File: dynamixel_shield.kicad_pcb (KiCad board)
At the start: 2 copper layers, 68.6 x 53.3 mm, 27 parts, among them P1 BARREL_JACK, P2 CONN_01X02, P3 CONN_01X03, P4 CONN_01X03, P5 CONN_01X03, P6 CONN_01X03, P7 CONN_01X03, P8 CONN_01X03, P9 CONN_01X03, Q1 MOSFET_N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

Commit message: change capacitor height (bom related only, footprint is the same)
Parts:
- C1: footprint Capacitors_SMD:c_elec_6.3x5.3 -> Capacitors_SMD:c_elec_6.3x5.8
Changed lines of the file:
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@@
     (links 61)
     (no_connects 0)
-    (area 53.318999 50.945 132.842001 112.522001)
+    (area 0 0 0 0)
     (thickness 1.6)
     (drawings 20)
@@
       (xy 0.633953 3.996765) (xy 0.746536 3.399573)) (layer B.Cu) (width 0.01))
   )
-  (module Capacitors_SMD:c_elec_6.3x5.3 (layer F.Cu)
-    (at 93.98 84.328)
-    (descr "SMT capacitor, aluminium electrolytic, 6.3x5.3")
-    (attr smd)
-    (fp_text reference C1 (at 0 -4.445) (layer F.SilkS)
-      (effects (font (size 1 1) (thickness 0.15)))
-    )
-    (fp_text value 47uF (at 0 4.445) (layer F.Fab)
-      (effects (font (size 1 1) (thickness 0.15)))
-    )
-    (fp_line (start -4.85 -3.65) (end 4.85 -3.65) (layer F.CrtYd) (width 0.05))
-    (fp_line (start 4.85 -3.65) (end 4.85 3.65) (layer F.CrtYd) (width 0.05))
-    (fp_line (start 4.85 3.65) (end -4.85 3.65) (layer F.CrtYd) (width 0.05))
-    (fp_line (start -4.85 3.65) (end -4.85 -3.65) (layer F.CrtYd) (width 0.05))
-    (fp_line (start -2.921 -0.762) (end -2.921 0.762) (layer F.SilkS) (width 0.15))
-    (fp_line (start -2.794 1.143) (end -2.794 -1.143) (layer F.SilkS) (width 0.15))
-    (fp_line (start -2.667 -1.397) (end -2.667 1.397) (layer F.SilkS) (width 0.15))
-    (fp_line (start -2.54 1.651) (end -2.54 -1.651) (layer F.SilkS) (width 0.15))
-    (fp_line (start -2.413 -1.778) (end -2.413 1.778) (layer F.SilkS) (width 0.15))
-    (fp_line (start -3.302 -3.302) (end -3.302 3.302) (layer F.SilkS) (width 0.15))
-    (fp_line (start -3.302 3.302) (end 2.54 3.302) (layer F.SilkS) (width 0.15))
-    (fp_line (start 2.54 3.302) (end 3.302 2.54) (layer F.SilkS) (width 0.15))
-    (fp_line (start 3.302 2.54) (end 3.302 -2.54) (layer F.SilkS) (width 0.15))
-    (fp_line (start 3.302 -2.54) (end 2.54 -3.302) (layer F.SilkS) (width 0.15))
-    (fp_line (start 2.54 -3.302) (end -3.302 -3.302) (layer F.SilkS) (width 0.15))
-    (fp_line (start 2.159 0) (end 1.397 0) (layer F.SilkS) (width 0.15))
-    (fp_line (start 1.778 -0.381) (end 1.778 0.381) (layer F.SilkS) (width 0.15))
-    (fp_circle (center 0 0) (end -3.048 0) (layer F.SilkS) (width 0.15))
-    (pad 1 smd rect (at 2.75082 0) (size 3.59918 1.6002) (layers F.Cu F.Paste F.Mask)
-      (net 9 +12V))
-    (pad 2 smd rect (at -2.75082 0) (size 3.59918 1.6002) (layers F.Cu F.Paste F.Mask)
-      (net 11 GND))
-    (model Capacitors_SMD.3dshapes/c_elec_6.3x5.3.wrl
-      (at (xyz 0 0 0))
-      (scale (xyz 1 1 1))
-      (rotate (xyz 0 0 0))
-    )
-  )
   (module Pin_Headers:Pin_Header_Straight_1x04 (layer F.Cu)
     (at 104.648 65.024 270)
@@
       (net 33 "Net-(SHIELD1-PadSCL)"))
   )
+  (module Capacitors_SMD:c_elec_6.3x5.8 (layer F.Cu)
+    (at 93.98 84.328)
+    (descr "SMT capacitor, aluminium electrolytic, 6.3x5.8")
+    (attr smd)
+    (fp_text reference C1 (at 0 -4.445) (layer F.SilkS)
+      (effects (font (size 1 1) (thickness 0.15)))
+    )
+    (fp_text value 47uF (at 0 4.445) (layer F.Fab)
+      (effects (font (size 1 1) (thickness 0.15)))
+    )
+    (fp_line (start -4.85 -3.65) (end 4.85 -3.7) (layer F.CrtYd) (width 0.05))
+    (fp_line (start 4.85 -3.7) (end 4.85 3.65) (layer F.CrtYd) (width 0.05))
+    (fp_line (start 4.85 3.65) (end -4.85 3.65) (layer F.CrtYd) (width 0.05))
+    (fp_line (start -4.85 3.65) (end -4.85 -3.65) (layer F.CrtYd) (width 0.05))
+    (fp_line (start -2.921 -0.762) (end -2.921 0.762) (layer F.SilkS) (width 0.15))
+    (fp_line (start -2.794 1.143) (end -2.794 -1.143) (layer F.SilkS) (width 0.15))
+    (fp_line (start -2.667 -1.397) (end -2.667 1.397) (layer F.SilkS) (width 0.15))
+    (fp_line (start -2.54 1.651) (end -2.54 -1.651) (layer F.SilkS) (width 0.15))
+    (fp_line (start -2.413 -1.778) (end -2.413 1.778) (layer F.SilkS) (width 0.15))
+    (fp_line (start -3.302 -3.302) (end -3.302 3.302) (layer F.SilkS) (width 0.15))
+    (fp_line (start -3.302 3.302) (end 2.54 3.302) (layer F.SilkS) (width 0.15))
+    (fp_line (start 2.54 3.302) (end 3.302 2.54) (layer F.SilkS) (width 0.15))
+    (fp_line (start 3.302 2.54) (end 3.302 -2.54) (layer F.SilkS) (width 0.15))
+    (fp_line (start 3.302 -2.54) (end 2.54 -3.302) (layer F.SilkS) (width 0.15))
+    (fp_line (start 2.54 -3.302) (end -3.302 -3.302) (layer F.SilkS) (width 0.15))
+    (fp_line (start 2.159 0) (end 1.397 0) (layer F.SilkS) (width 0.15))
+    (fp_line (start 1.778 -0.381) (end 1.778 0.381) (layer F.SilkS) (width 0.15))
+    (fp_circle (center 0 0) (end -3.048 0) (layer F.SilkS) (width 0.15))
+    (pad 1 smd rect (at 2.75082 0) (size 3.59918 1.6002) (layers F.Cu F.Paste F.Mask)
+      (net 9 +12V))
+    (pad 2 smd rect (at -2.75082 0) (size 3.59918 1.6002) (layers F.Cu F.Paste F.Mask)
+      (net 11 GND))
+    (model Capacitors_SMD.3dshapes/c_elec_6.3x5.8.wrl
+      (at (xyz 0 0 0))
+      (scale (xyz 1 1 1))
+      (rotate (xyz 0 0 0))
+    )
+  )
   (gr_text EXT (at 115.57 65.532 90) (layer F.SilkS)

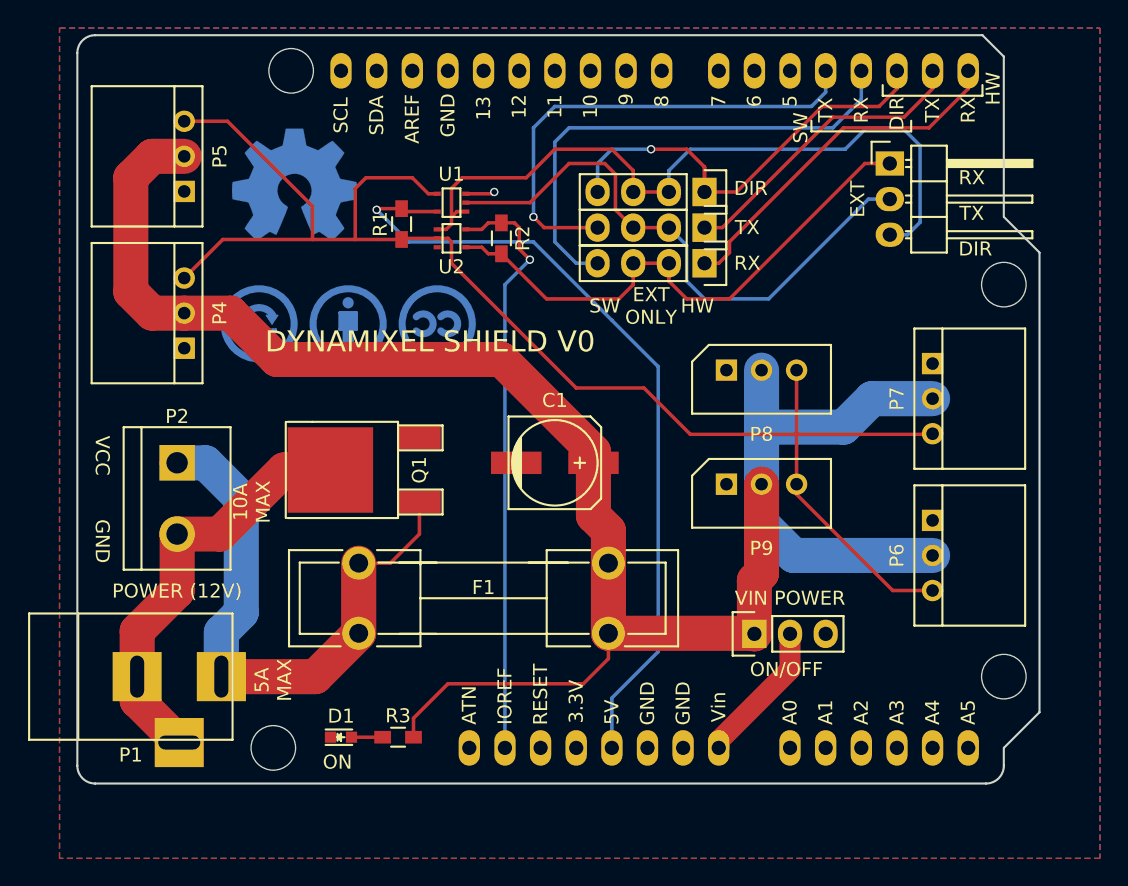
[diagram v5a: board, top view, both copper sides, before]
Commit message: fix a few shortcomings of the pcb, thanks to tautech from eevblog forum
remove potential acid trap between p8 and p9
increase pad size of molex connectors
move polarity indicators to be visible
increase led pad size for easier soldering
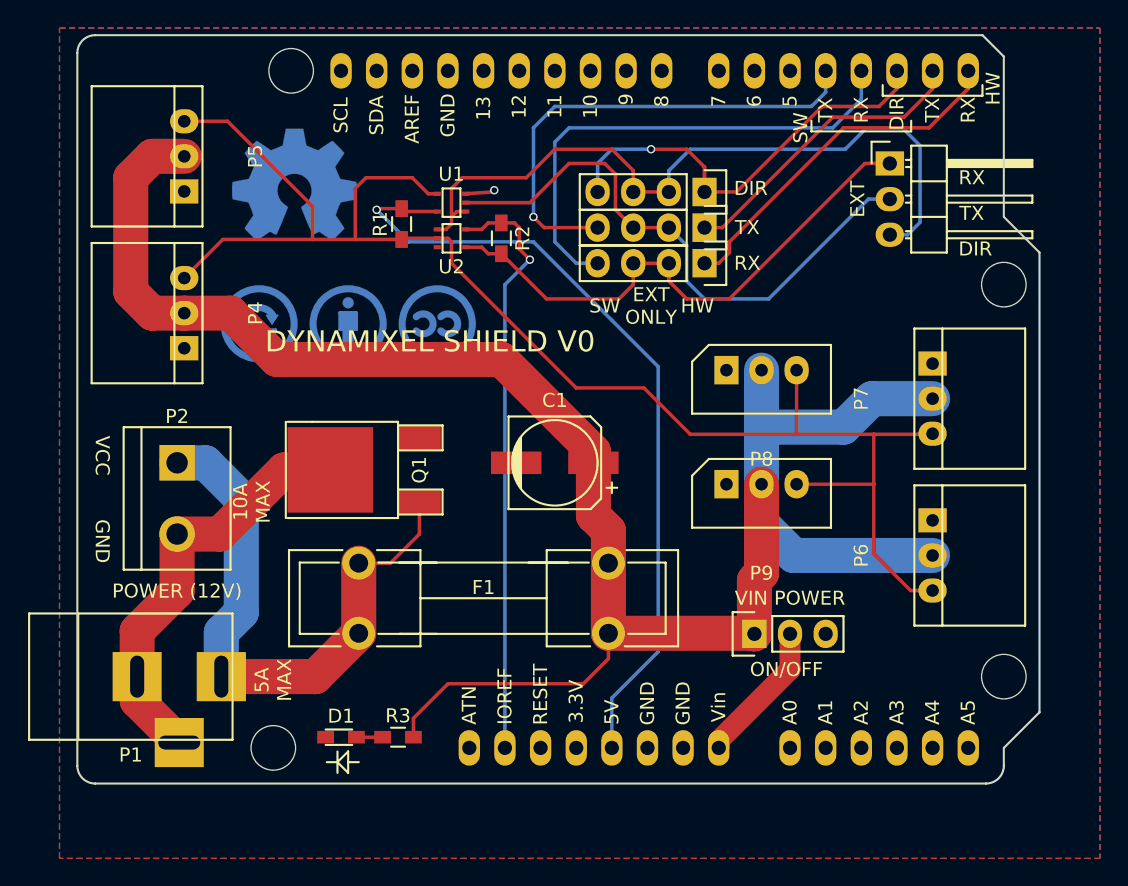
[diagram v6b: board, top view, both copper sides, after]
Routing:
- net /DATA: track 107.0 -> 109.5 mm
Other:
- board text removed: "ON"

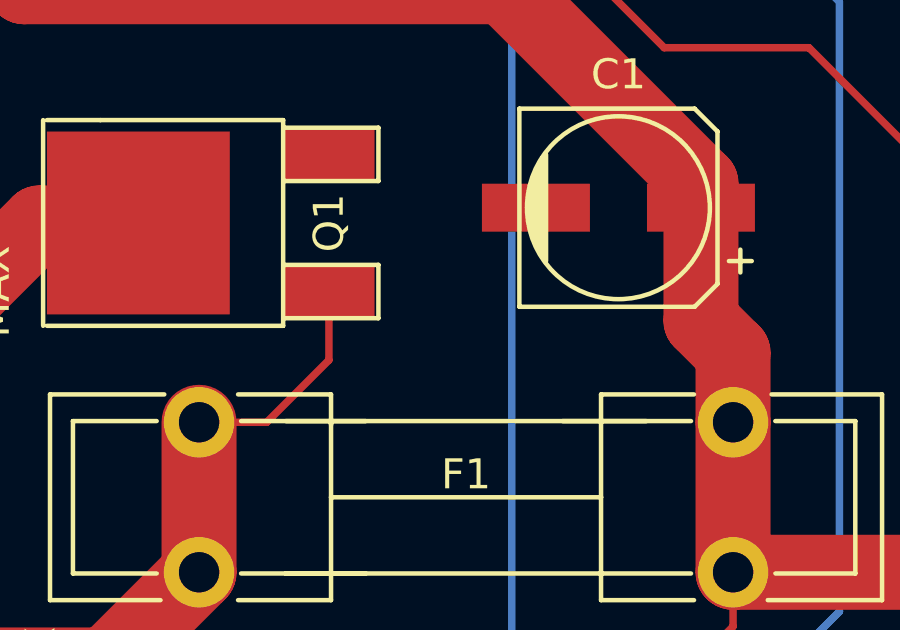
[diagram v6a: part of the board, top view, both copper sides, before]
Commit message: put the fuse before the reverse voltage protection (thanks to bktemp from eevblog forum)
Quoting bktemp user on eevblog:

When the fuse fails, there will be a voltage spike.
Since there is no load except the mosfet gate, the voltage spike will damage the mosfet,
maybe even shorting gate-source and therefore the input supply.
If the gate is connected after the fuse, is will be connected in parallel with C1,
providing some protection for the sensitive gate.
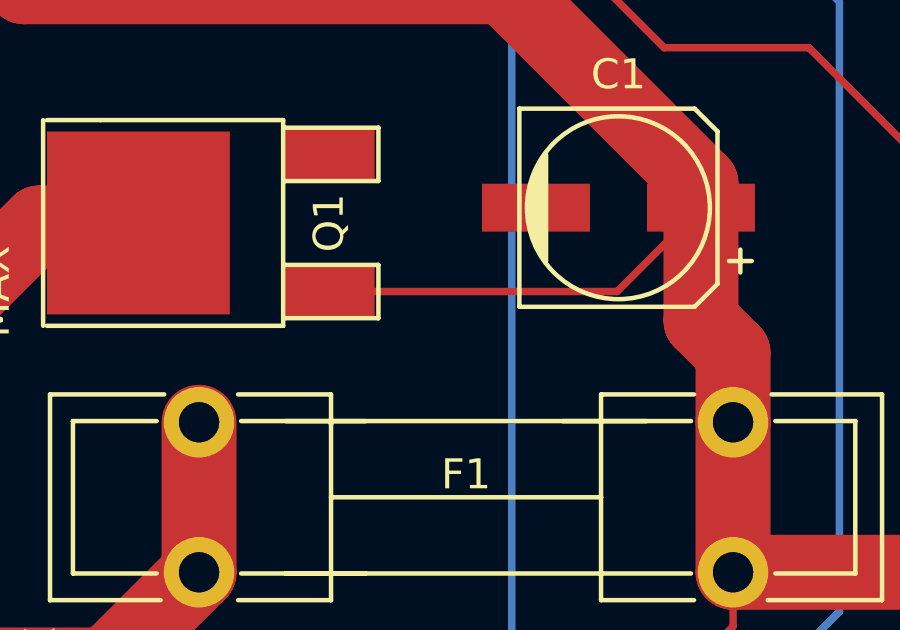
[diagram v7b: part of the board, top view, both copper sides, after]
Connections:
- Q1 pad 1: Net-(F1-Pad1) -> +12V
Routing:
- net +12V: track 140.9 -> 154.4 mm
- net Net-(F1-Pad1): track 42.5 -> 35.0 mm
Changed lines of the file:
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@@
     (links 61)
     (no_connects 0)
-    (area 53.318999 50.945 132.842001 112.522001)
+    (area 0 0 0 0)
     (thickness 1.6)
     (drawings 19)
-    (tracks 205)
+    (tracks 204)
     (zones 0)
     (modules 27)
@@
     (fp_line (start 3.429 -9.398) (end 3.429 -7.62) (layer F.SilkS) (width 0.15))
     (pad 1 smd rect (at -2.286 0 90) (size 1.651 3.048) (layers F.Cu F.Paste F.Mask)
-      (net 37 "Net-(F1-Pad1)"))
+      (net 9 +12V))
     (pad 2 smd rect (at 0 -6.35 90) (size 6.096 6.096) (layers F.Cu F.Paste F.Mask)
       (net 38 "Net-(P1-Pad2)"))
@@
   (segment (start 113.792 60.452) (end 94.996 60.452) (width 0.25) (layer B.Cu) (net 8))
   (segment (start 115.824 58.42) (end 113.792 60.452) (width 0.25) (layer B.Cu) (net 8))
+  (segment (start 84.328 87.122) (end 93.93682 87.122) (width 0.25) (layer F.Cu) (net 9))
+  (segment (start 93.93682 87.122) (end 96.73082 84.328) (width 0.25) (layer F.Cu) (net 9))
   (segment (start 83.904 103.886) (end 83.904 102.532) (width 0.25) (layer F.Cu) (net 9))
   (segment (start 97.8 98.288) (end 97.8 96.48) (width 0.25) (layer F.Cu) (net 9))
@@
   (segment (start 85.598 66.421) (end 83.269 66.421) (width 0.25) (layer F.Cu) (net 14))
   (segment (start 83.269 66.421) (end 83.058 66.21) (width 0.25) (layer F.Cu) (net 14))
-  (segment (start 84.328 87.122) (end 84.328 89.408) (width 0.25) (layer F.Cu) (net 37))
-  (segment (start 82.256 91.48) (end 80 91.48) (width 0.25) (layer F.Cu) (net 37))
-  (segment (start 84.328 89.408) (end 82.256 91.48) (width 0.25) (layer F.Cu) (net 37))
   (segment (start 70.20814 99.568) (end 76.912 99.568) (width 2.5) (layer F.Cu) (net 37))
   (segment (start 76.912 99.568) (end 80 96.48) (width 2.5) (layer F.Cu) (net 37))
@@
   (segment (start 67.056 93.472) (end 67.056 89.408) (width 2.5) (layer F.Cu) (net 38))
   (segment (start 64.20866 96.31934) (end 67.056 93.472) (width 2.5) (layer F.Cu) (net 38))
-  (segment (start 79.84 103.886) (end 81.704 103.886) (width 0.25) (layer F.Cu) (net 39) (status C00000))
+  (segment (start 79.84 103.886) (end 81.704 103.886) (width 0.25) (layer F.Cu) (net 39))
   (zone (net 11) (net_name GND) (layer F.Cu) (hatch edge 0.508)
     (connect_pads (clearance 0.254))

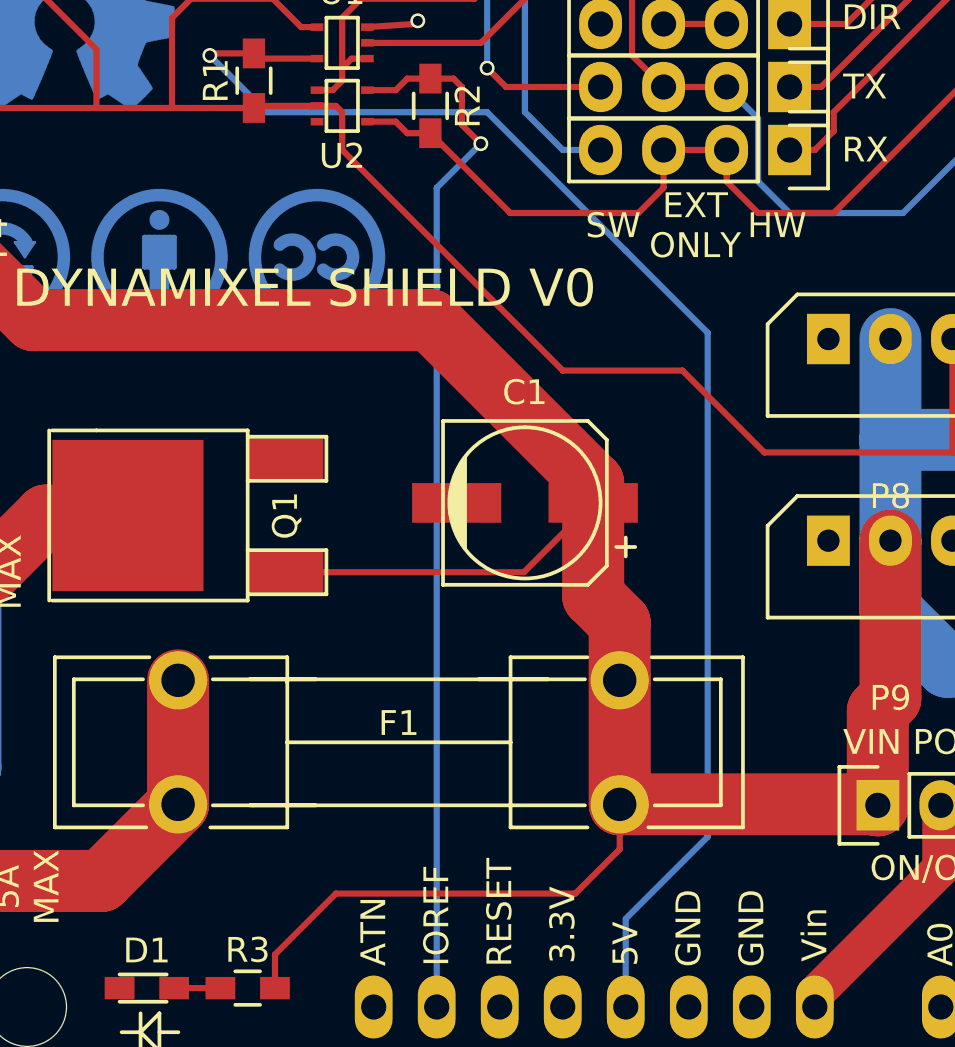
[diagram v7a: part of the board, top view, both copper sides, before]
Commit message: add a few vias between ground planes (suggested by bson from eevblog)
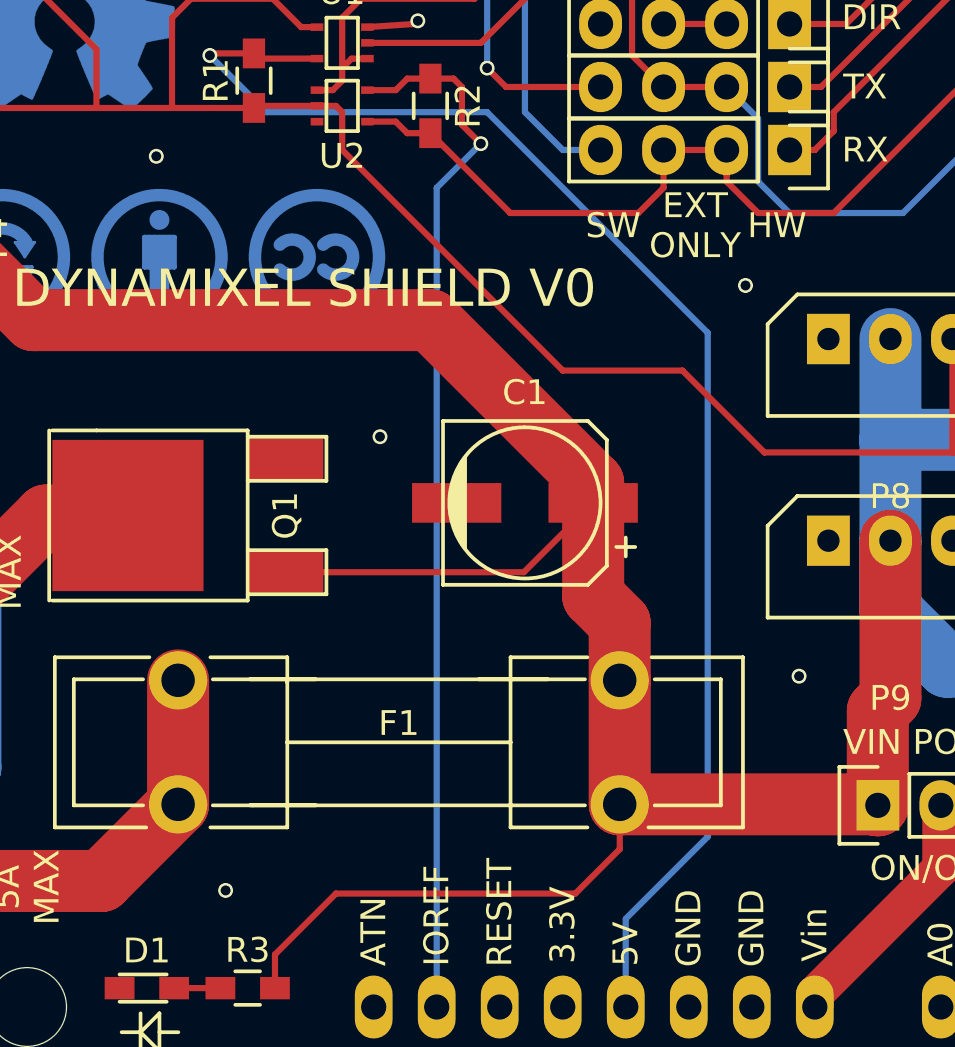
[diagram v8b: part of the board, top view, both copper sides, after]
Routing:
- net GND: vias 1 -> 6
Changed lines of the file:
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@@
     (links 61)
     (no_connects 0)
-    (area 0 0 0 0)
+    (area 53.318999 50.945 132.842001 112.522001)
     (thickness 1.6)
     (drawings 19)
-    (tracks 204)
+    (tracks 209)
     (zones 0)
     (modules 27)
@@
   (layers
     (0 F.Cu signal)
-    (31 B.Cu signal hide)
+    (31 B.Cu signal)
     (32 B.Adhes user hide)
     (33 F.Adhes user hide)
@@
   (segment (start 110.744 99.06) (end 105.664 104.14) (width 1.5) (layer F.Cu) (net 10))
   (segment (start 105.664 104.14) (end 105.664 104.648) (width 1.5) (layer F.Cu) (net 10))
+  (via (at 102.87 75.565) (size 0.6) (drill 0.4) (layers F.Cu B.Cu) (net 11))
+  (via (at 105.029 91.313) (size 0.6) (drill 0.4) (layers F.Cu B.Cu) (net 11))
+  (via (at 81.915 99.949) (size 0.6) (drill 0.4) (layers F.Cu B.Cu) (net 11))
+  (via (at 88.138 81.661) (size 0.6) (drill 0.4) (layers F.Cu B.Cu) (net 11))
+  (via (at 79.121 70.358) (size 0.6) (drill 0.4) (layers F.Cu B.Cu) (net 11))
   (segment (start 87.63 65.151) (end 89.535 65.024) (width 0.25) (layer F.Cu) (net 11))
   (via (at 89.662 64.897) (size 0.6) (drill 0.4) (layers F.Cu B.Cu) (net 11))
